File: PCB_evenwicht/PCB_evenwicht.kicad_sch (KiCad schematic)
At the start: 34 parts, among them IC1 A4988SETTR-T, J1 Conn_01x04_Pin, J2 Barrel_Jack, J3 Conn_01x04_Pin, J4 Conn_01x03_Pin, J5 Conn_01x02_Pin, SW1 EN, SW2 FLASH, U1 ESP32-WROOM-32, U2 AMS1117-3.3, U3 MP1584

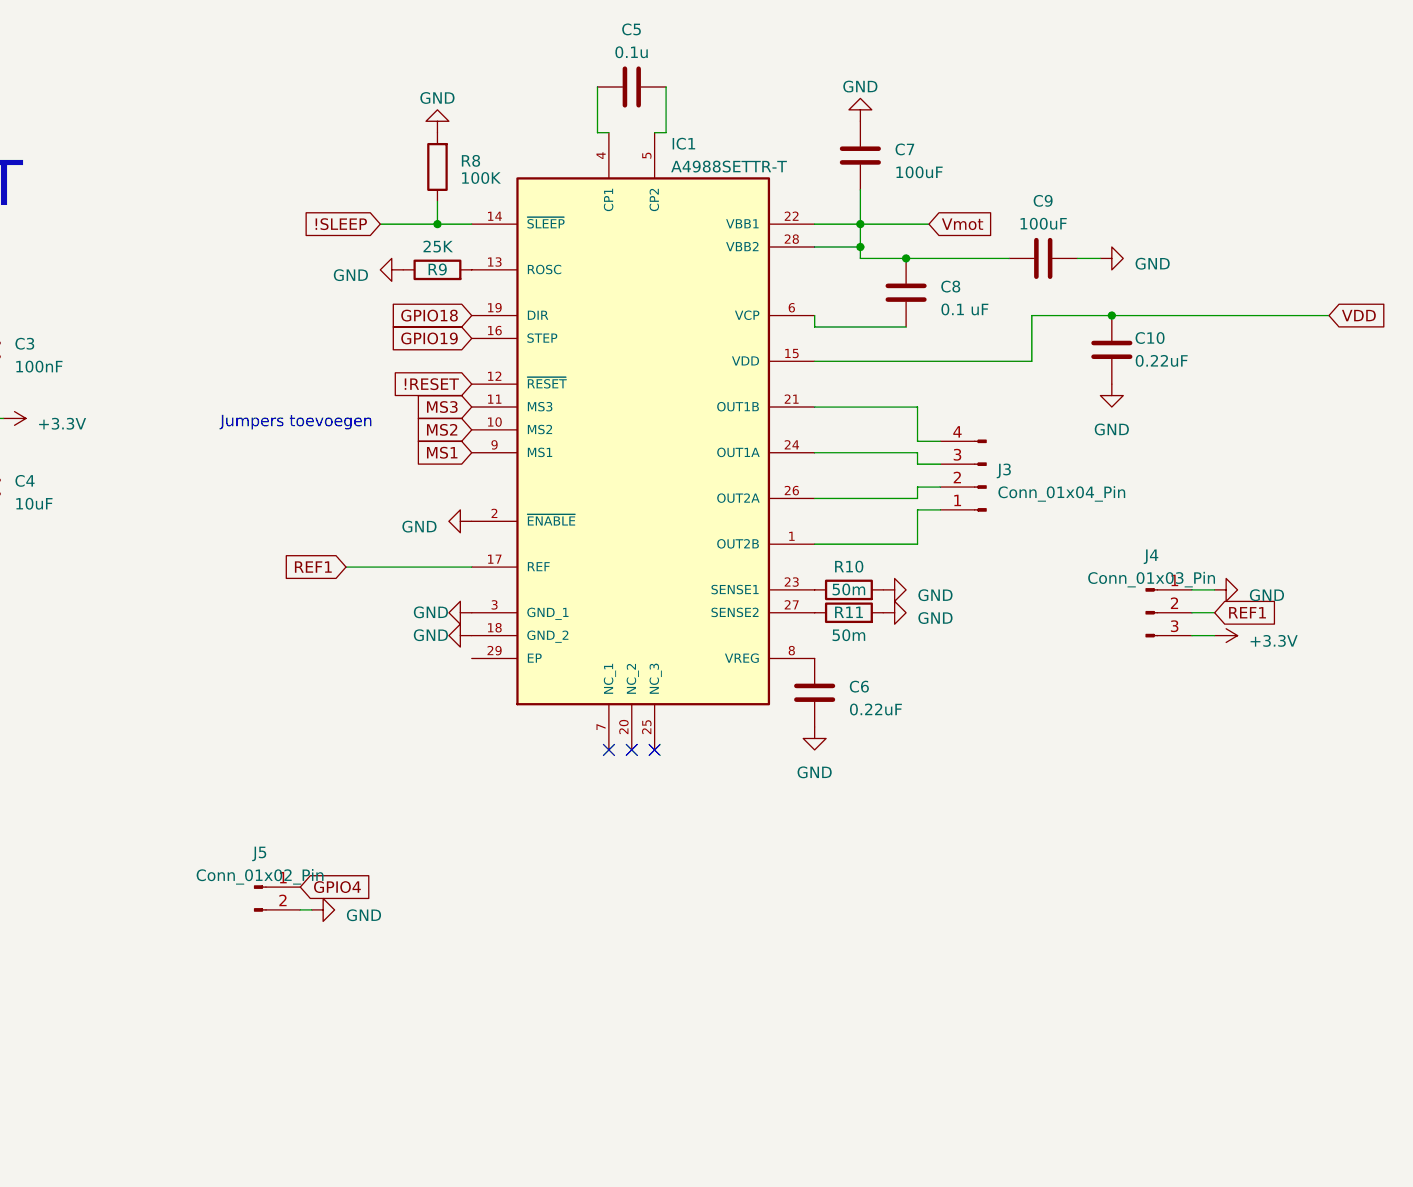
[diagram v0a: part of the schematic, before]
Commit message: PCB_Update
Nog enkel de footprints van de controller aanduiden en controleren van de waarden
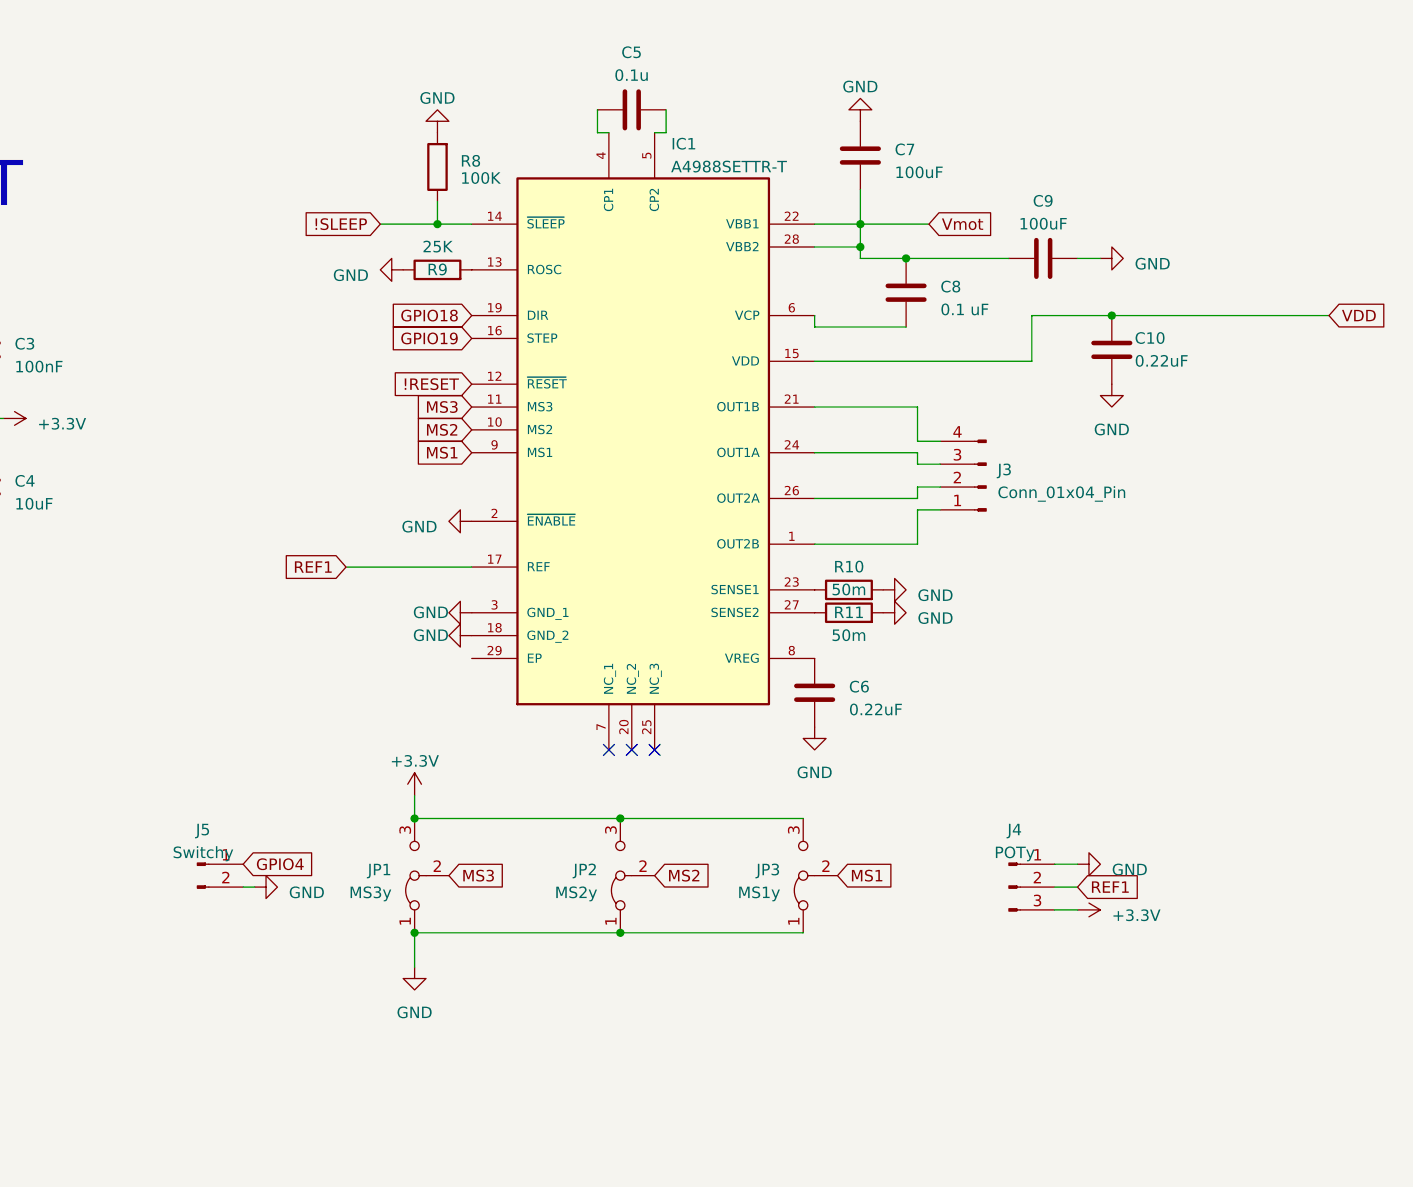
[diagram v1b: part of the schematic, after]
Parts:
- added JP1: MS3y, Jumper:SolderJumper-3_P1.3mm_Open_Pad1.0x1.5mm, symbol Jumper:Jumper_3_Bridged12
- added JP2: MS2y, Jumper:SolderJumper-3_P1.3mm_Open_Pad1.0x1.5mm, symbol Jumper:Jumper_3_Bridged12
- added JP3: MS1y, Jumper:SolderJumper-3_P1.3mm_Open_Pad1.0x1.5mm, symbol Jumper:Jumper_3_Bridged12
- J4: value Conn_01x03_Pin -> POTy; footprint (none) -> Connector_PinHeader_2.54mm:PinHeader_1x03_P2.54mm_Vertical
- J5: value Conn_01x02_Pin -> Switchy; footprint (none) -> Connector_PinHeader_2.54mm:PinHeader_1x02_P2.54mm_Vertical
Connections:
- net +3.3V: now also JP1.3 (B), JP2.3 (B), JP3.3 (B)
- net GND: now also JP1.1 (A), JP2.1 (A), JP3.1 (A)
- net MS1: now also JP3.2 (C)
- net MS2: now also JP2.2 (C)
- net MS3: now also JP1.2 (C)
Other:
- note removed: "Jumpers toevoegen"
- moved on the sheet: C5, J4, J5

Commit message: update
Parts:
- renumbered J2 to J1, J1 to J2, J5 to J3, J3 to J4, J4 to J5, R11 to R10, R10 to R11
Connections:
- net +3.3V: now also R8.2
- net GND: no longer R8.2
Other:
- note added: "NOG een 4.7uf condensator denk ik ergens plaatsen"
- moved on the sheet: R10, R11

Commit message: update
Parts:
- removed C1: 100uF/6.3V, Capacitor_SMD:C_0805_2012Metric_Pad1.18x1.45mm_HandSolder, symbol Device:C
- removed C10, C6: 0.22uF, symbol Device:C
- removed C2, C4: 10uF, Capacitor_SMD:C_0805_2012Metric_Pad1.18x1.45mm_HandSolder, symbol Device:C
- removed C3: 100nF, Capacitor_SMD:C_0805_2012Metric_Pad1.18x1.45mm_HandSolder, symbol Device:C
- removed C5: 0.1u, symbol Device:C
- removed C7, C9: 100uF, symbol Device:C
- removed C8: 0.1 uF, symbol Device:C
- removed D1: BLUE, LED_SMD:LED_0805_2012Metric_Pad1.15x1.40mm_HandSolder, symbol Device:LED
- removed D2: PWR, LED_SMD:LED_0805_2012Metric_Pad1.15x1.40mm_HandSolder, symbol Device:LED
- removed IC1: A4988SETTR-T, A4988:QFN50P500X500X100-29N, symbol A4988SETTR-T:A4988SETTR-T
- removed J1: Barrel_Jack, Connector_BarrelJack:BarrelJack_GCT_DCJ200-10-A_Horizontal, symbol Connector:Barrel_Jack
- removed J2, J4: Conn_01x04_Pin, Connector_PinHeader_2.54mm:PinHeader_1x04_P2.54mm_Vertical, symbol Connector:Conn_01x04_Pin
- removed R1, R2, R3, R5, R6: 10K, Resistor_SMD:R_0805_2012Metric_Pad1.20x1.40mm_HandSolder, symbol Device:R
- removed R10, R11: 50m, symbol Device:R
- removed R4, R7: 1K, Resistor_SMD:R_0805_2012Metric_Pad1.20x1.40mm_HandSolder, symbol Device:R
- removed R8: 100K, symbol Device:R
- removed R9: 25K, symbol Device:R
- removed SW1: EN, Button_Switch_SMD:SW_DIP_SPSTx01_Slide_Copal_CHS-01B_W7.62mm_P1.27mm, symbol Switch:SW_Push
- removed SW2: FLASH, Button_Switch_SMD:SW_DIP_SPSTx01_Slide_Copal_CHS-01B_W7.62mm_P1.27mm, symbol Switch:SW_Push
- removed U1: ESP32-WROOM-32, RF_Module:ESP32-WROOM-32, symbol RF_Module:ESP32-WROOM-32
- removed U2: AMS1117-3.3, Package_TO_SOT_SMD:SOT-223-3_TabPin2, symbol Regulator_Linear:AMS1117-3.3
- removed U3: MP1584, Library:U1584, symbol Lib:MP1584
- added J7: Switchx, Connector_PinHeader_2.54mm:PinHeader_1x02_P2.54mm_Vertical, symbol Connector:Conn_01x02_Pin
- added J8: POTx, Connector_PinHeader_2.54mm:PinHeader_1x03_P2.54mm_Vertical, symbol Connector:Conn_01x03_Pin
- added J9: Switch_einde, Connector_PinHeader_2.54mm:PinHeader_1x02_P2.54mm_Vertical, symbol Connector:Conn_01x02_Pin
- added JP4: MS3x, Jumper:SolderJumper-3_P1.3mm_Open_Pad1.0x1.5mm, symbol Jumper:Jumper_3_Bridged12
- added JP5: MS2x, Jumper:SolderJumper-3_P1.3mm_Open_Pad1.0x1.5mm, symbol Jumper:Jumper_3_Bridged12
- added JP6: MS1x, Jumper:SolderJumper-3_P1.3mm_Open_Pad1.0x1.5mm, symbol Jumper:Jumper_3_Bridged12
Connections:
- net +3.3V: now also J8.3 (Pin_3), JP4.3 (B), JP5.3 (B), JP6.3 (B)
- net GND: now also J7.2 (Pin_2), J8.1 (Pin_1), J9.2 (Pin_2), JP4.1 (A), JP5.1 (A), JP6.1 (A)
- net GPIO14: now also J7.1 (Pin_1)
- net MS1 renamed MS1_1
- net MS1_1: now also JP6.2 (C)
- net MS2 renamed MS2_1
- net MS2_1: now also JP5.2 (C)
- net MS3 renamed MS3_1
- net MS3_1: now also JP4.2 (C)
- new net GPIO27.: J9.1 (Pin_1)
- new net REF2: J8.2 (Pin_2)
- no-connect marks 9 -> 0
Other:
- added sheet A4988_1 (a4988_1.kicad_sch)
- added sheet A4988_2 (a4988_2.kicad_sch)
- added sheet ESP32 (esp32.kicad_sch)
- note removed: "NOG een 4.7uf condensator denk ik ergens plaatsen"
- note removed: "POWER PART"
- moved on the sheet: J3, J5, JP1, JP2, JP3

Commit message: update
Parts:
- added C2, C4: 10uF, Capacitor_SMD:C_0805_2012Metric_Pad1.18x1.45mm_HandSolder, symbol Device:C
- added C3: 100nF, Capacitor_SMD:C_0805_2012Metric_Pad1.18x1.45mm_HandSolder, symbol Device:C
- added J1: Barrel_Jack, Connector_BarrelJack:BarrelJack_GCT_DCJ200-10-A_Horizontal, symbol Connector:Barrel_Jack
- added U2: AMS1117-3.3, Package_TO_SOT_SMD:SOT-223-3_TabPin2, symbol Regulator_Linear:AMS1117-3.3
- added U3: MP1584, Library:U1584, symbol Lib:MP1584
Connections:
- net +3.3V: now also C3.2, C4.1, U2.2 (VO)
- net GND: now also C2.2, C3.1, C4.2, U2.1 (GND), U3.7 (OUT-), U3.8 (OUT-)
- net GPIO27. renamed GPIO27
- new net: J1.2, U3.1 (IN-), U3.2 (IN-)
- new net VDD: C2.1, U2.3 (VI), U3.5 (OUT+), U3.6 (OUT+)
- new net Vmot: J1.1, U3.3 (IN+), U3.4 (IN+)
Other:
- note added: "POWER PART"

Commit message: klj
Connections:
- net MS1_1: no longer JP6.2 (C)
- net MS2_1: no longer JP5.2 (C)
- net MS3_1: no longer JP4.2 (C)
- new net MS1_2: JP6.2 (C)
- new net MS2_2: JP5.2 (C)
- new net MS3_2: JP4.2 (C)
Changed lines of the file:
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@@
     )
   )
-  (global_label "MS1_1" (shape input) (at 100.33 101.6 0) (fields_autoplaced)
+  (global_label "MS1_2" (shape input) (at 100.33 101.6 0) (fields_autoplaced)
     (effects (font (size 1.27 1.27)) (justify left))
     (property "Intersheetrefs" "${INTERSHEET_REFS}" (at 109.2833 101.6 0)
@@
     )
   )
-  (global_label "MS2_1" (shape input) (at 80.01 101.6 0) (fields_autoplaced)
+  (global_label "MS2_2" (shape input) (at 80.01 101.6 0) (fields_autoplaced)
     (effects (font (size 1.27 1.27)) (justify left))
     (property "Intersheetrefs" "${INTERSHEET_REFS}" (at 88.9633 101.6 0)
@@
     )
   )
-  (global_label "MS3_1" (shape input) (at 57.15 101.6 0) (fields_autoplaced)
+  (global_label "MS3_2" (shape input) (at 57.15 101.6 0) (fields_autoplaced)
     (effects (font (size 1.27 1.27)) (justify left))
     (property "Intersheetrefs" "${INTERSHEET_REFS}" (at 66.1033 101.6 0)

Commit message: fdq
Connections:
- net GPIO4 is gone; now on net GPIO14: J3.1 (Pin_1)
- net GPIO14: no longer J7.1 (Pin_1)
- net GPIO27: now also J7.1 (Pin_1); no longer J9.1 (Pin_1)
- net REF1 renamed A9
- net REF2 renamed A8
- new net GPIO12: J9.1 (Pin_1)
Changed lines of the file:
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@@
     )
   )
-  (global_label "GPIO27" (shape input) (at 33.02 43.18 0) (fields_autoplaced)
+  (global_label "GPIO12" (shape input) (at 33.02 43.18 0) (fields_autoplaced)
     (effects (font (size 1.27 1.27)) (justify left))
     (property "Intersheetrefs" "${INTERSHEET_REFS}" (at 42.8201 43.18 0)
@@
     )
   )
-  (global_label "REF1" (shape input) (at 127 68.58 0) (fields_autoplaced)
+  (global_label "A9" (shape input) (at 127 68.58 0) (fields_autoplaced)
     (effects (font (size 1.27 1.27)) (justify left))
-    (property "Intersheetrefs" "${INTERSHEET_REFS}" (at 134.6229 68.58 0)
+    (property "Intersheetrefs" "${INTERSHEET_REFS}" (at 132.2039 68.58 0)
       (effects (font (size 1.27 1.27)) (justify left) hide)
     )
   )
-  (global_label "REF2" (shape input) (at 127 102.87 0) (fields_autoplaced)
+  (global_label "A8" (shape input) (at 127 102.87 0) (fields_autoplaced)
     (effects (font (size 1.27 1.27)) (justify left))
-    (property "Intersheetrefs" "${INTERSHEET_REFS}" (at 134.6229 102.87 0)
+    (property "Intersheetrefs" "${INTERSHEET_REFS}" (at 132.2039 102.87 0)
       (effects (font (size 1.27 1.27)) (justify left) hide)
     )
@@
     )
   )
-  (global_label "GPIO4" (shape input) (at 34.29 66.04 0) (fields_autoplaced)
+  (global_label "GPIO14" (shape input) (at 34.29 66.04 0) (fields_autoplaced)
     (effects (font (size 1.27 1.27)) (justify left))
-    (property "Intersheetrefs" "${INTERSHEET_REFS}" (at 42.8806 66.04 0)
+    (property "Intersheetrefs" "${INTERSHEET_REFS}" (at 44.0901 66.04 0)
       (effects (font (size 1.27 1.27)) (justify left) hide)
     )
   )
-  (global_label "GPIO14" (shape input) (at 34.29 100.33 0) (fields_autoplaced)
+  (global_label "GPIO27" (shape input) (at 34.29 100.33 0) (fields_autoplaced)
     (effects (font (size 1.27 1.27)) (justify left))
     (property "Intersheetrefs" "${INTERSHEET_REFS}" (at 44.0901 100.33 0)
